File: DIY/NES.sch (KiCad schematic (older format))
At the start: 9 parts, among them J1 Conn_01x07, J2 Conn_01x07, J3 DB15_Female, J4 DB25_Male, U1 74AHCT125N, U2 74AHCT125N

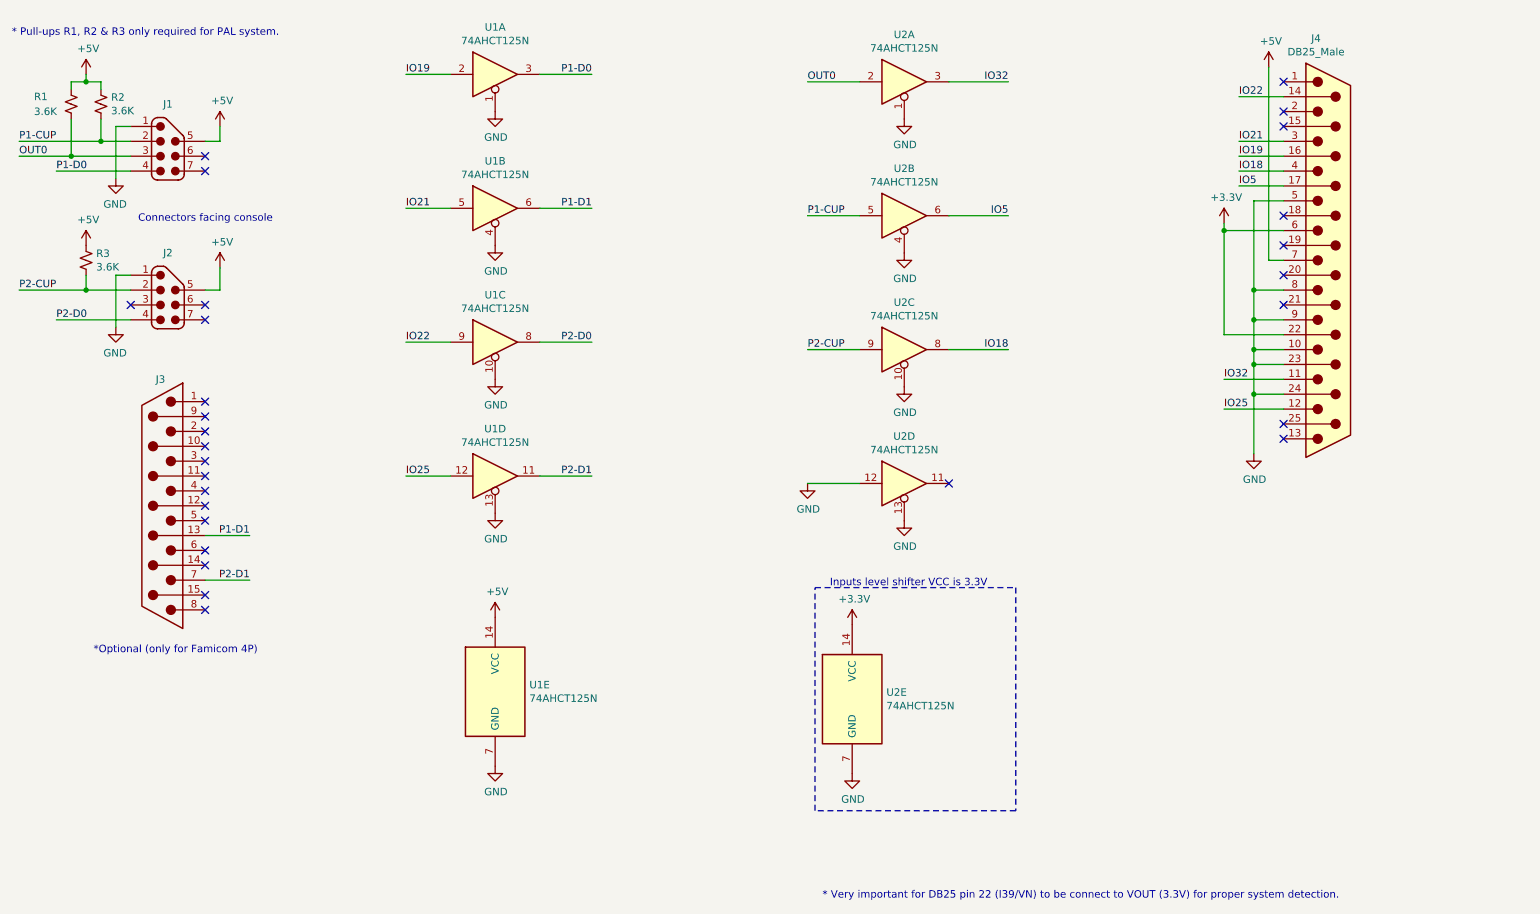
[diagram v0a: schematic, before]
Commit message: Split NES and FC schematic into 3 types
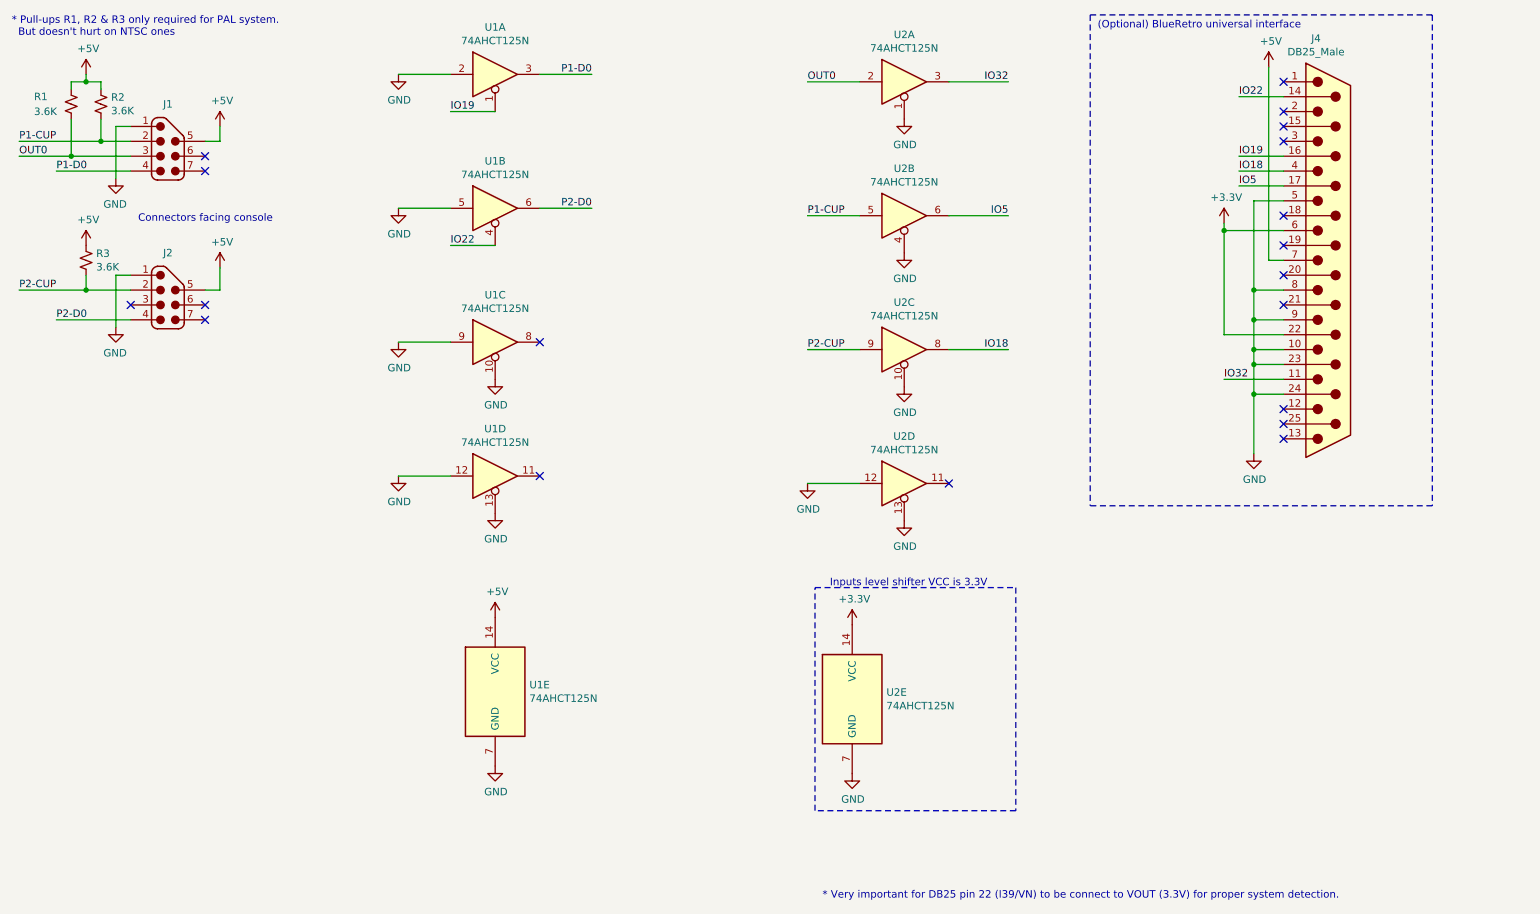
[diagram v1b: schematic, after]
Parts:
- removed J3: DB15_Female, symbol Connector_Gaming:Atari5200_Famicom_NeoGeoAES_PCGamePort_DA15
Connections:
- net P1-D1 is gone; now on net P2-D0: U1.6
- net GND: now also U1.12, U1.2, U1.5, U1.9; no longer U1.1, U1.4
- net IO19: now also U1.1; no longer U1.2
- net IO22: now also U1.4; no longer U1.9
- net P2-D0: no longer U1.8
- net IO21: no longer names the net of J4.3
- net IO21: no longer U1.5
- net IO25: no longer names the net of J4.12
- net IO25: no longer U1.12
- net P2-D1: no longer names the net of U1.11
- no-connect marks 28 -> 19
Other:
- note added: "(Optional) BlueRetro universal interface"
- note added: "* Pull-ups R1, R2 & R3 only required for PAL system.\n But doesn't hurt on NTSC ones"
- note removed: "* Pull-ups R1, R2 & R3 only required for PAL system."
- note removed: "*Optional (only for Famicom 4P)"
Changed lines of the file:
@@
 $Descr USLetter 11000 8500
 encoding utf-8
-Sheet 3 21
-Title "BlueRetro - Famicom/NES adapter cable"
+Sheet 3 23
+Title "BlueRetro - NES adapter cable"
 Date "2020-11-03"
-Rev "v1.2.1"
+Rev "v1.3"
 Comp "©2020-2022 Jacques Gagnon, licensed under CC-BY-4.0"
 Comment1 ""
@@
 $Comp
 L 74xx:74LS125 U?
-U 2 1 5F23BC86
-P 4150 2250
-AR Path="/5F127084/5F23BC86" Ref="U?"  Part="2"
-AR Path="/5F1E85DD/5F23BC86" Ref="U1"  Part="2"
-F 0 "U1" H 4150 2567 50  0000 C CNN
-F 1 "74AHCT125N" H 4150 2476 50  0000 C CNN
-F 2 "" H 4150 2250 50  0001 C CNN
-F 3 "http://www.ti.com/lit/gpn/sn74LS125" H 4150 2250 50  0001 C CNN
-	2    4150 2250
-	1    0    0    -1
-$EndComp
-$Comp
-L 74xx:74LS125 U?
-U 3 1 5F23BC8C
-P 4150 3150
-AR Path="/5F127084/5F23BC8C" Ref="U?"  Part="3"
-AR Path="/5F1E85DD/5F23BC8C" Ref="U1"  Part="3"
-F 0 "U1" H 4150 3467 50  0000 C CNN
-F 1 "74AHCT125N" H 4150 3376 50  0000 C CNN
-F 2 "" H 4150 3150 50  0001 C CNN
-F 3 "http://www.ti.com/lit/gpn/sn74LS125" H 4150 3150 50  0001 C CNN
-	3    4150 3150
-	1    0    0    -1
-$EndComp
-$Comp
-L 74xx:74LS125 U?
 U 4 1 5F23BC92
 P 4150 4050
@@
 F 3 "" H 6900 2550 50  0001 C CNN
 	1    6900 2550
-	1    0    0    -1
-$EndComp
-$Comp
-L power:GND #PWR?
-U 1 1 5F23BD36
-P 4150 2500
-AR Path="/5F127084/5F23BD36" Ref="#PWR?"  Part="1"
-AR Path="/5F1E85DD/5F23BD36" Ref="#PWR049"  Part="1"
-F 0 "#PWR049" H 4150 2250 50  0001 C CNN
-F 1 "GND" H 4155 2327 50  0000 C CNN
-F 2 "" H 4150 2500 50  0001 C CNN
-F 3 "" H 4150 2500 50  0001 C CNN
-	1    4150 2500
-	1    0    0    -1
-$EndComp
-$Comp
-L power:GND #PWR?
-U 1 1 5F23BD3C
-P 4150 4300
-AR Path="/5F127084/5F23BD3C" Ref="#PWR?"  Part="1"
-AR Path="/5F1E85DD/5F23BD3C" Ref="#PWR051"  Part="1"
-F 0 "#PWR051" H 4150 4050 50  0001 C CNN
-F 1 "GND" H 4155 4127 50  0000 C CNN
-F 2 "" H 4150 4300 50  0001 C CNN
-F 3 "" H 4150 4300 50  0001 C CNN
-	1    4150 4300
-	1    0    0    -1
-$EndComp
-$Comp
-L power:GND #PWR?
-U 1 1 5F23BD42
-P 4150 1600
-AR Path="/5F127084/5F23BD42" Ref="#PWR?"  Part="1"
-AR Path="/5F1E85DD/5F23BD42" Ref="#PWR048"  Part="1"
-F 0 "#PWR048" H 4150 1350 50  0001 C CNN
-F 1 "GND" H 4155 1427 50  0000 C CNN
-F 2 "" H 4150 1600 50  0001 C CNN
-F 3 "" H 4150 1600 50  0001 C CNN
-	1    4150 1600
-	1    0    0    -1
-$EndComp
-$Comp
-L power:GND #PWR?
-U 1 1 5F23BD48
-P 4150 3400
-AR Path="/5F127084/5F23BD48" Ref="#PWR?"  Part="1"
-AR Path="/5F1E85DD/5F23BD48" Ref="#PWR050"  Part="1"
-F 0 "#PWR050" H 4150 3150 50  0001 C CNN
-F 1 "GND" H 4155 3227 50  0000 C CNN
-F 2 "" H 4150 3400 50  0001 C CNN
-F 3 "" H 4150 3400 50  0001 C CNN
-	1    4150 3400
 	1    0    0    -1
 $EndComp
@@
 Inputs level shifter VCC is 3.3V
 Wire Wire Line
-	3850 1350 3550 1350
-Wire Wire Line
-	3850 2250 3550 2250
-Wire Wire Line
-	3850 3150 3550 3150
-Wire Wire Line
-	3850 4050 3550 4050
+	4150 1600 3850 1600
 Wire Wire Line
 	4450 1350 4800 1350
-Wire Wire Line
-	4450 2250 4800 2250
-Wire Wire Line
-	4450 3150 4800 3150
-Wire Wire Line
-	4450 4050 4800 4050
 Wire Wire Line
 	6600 1400 6250 1400
@@
 	1    0    0    -1
 $EndComp
-$Comp
-L Connector_Gaming:Atari5200_Famicom_NeoGeoAES_PCGamePort_DA15 J3
-U 1 1 5F2B655C
-P 1900 4250
-F 0 "J3" H 1900 3400 50  0000 C CNN
-F 1 "DB15_Female" H 1806 5151 50  0001 C CNN
-F 2 "" H 1900 4250 50  0001 C CNN
-F 3 " ~" H 1900 4250 50  0001 C CNN
-	1    1900 4250
-	-1   0    0    1
-$EndComp
-Wire Wire Line
-	2200 4450 2500 4450
-Wire Wire Line
-	2200 4750 2500 4750
-Text Notes 1450 5250 0    50   ~ 0
-*Optional (only for Famicom 4P)
-NoConn ~ 2200 3550
-NoConn ~ 2200 3650
-NoConn ~ 2200 3750
-NoConn ~ 2200 3850
-NoConn ~ 2200 3950
-NoConn ~ 2200 4050
-NoConn ~ 2200 4150
-NoConn ~ 2200 4250
-NoConn ~ 2200 4350
-NoConn ~ 2200 4550
-NoConn ~ 2200 4650
-NoConn ~ 2200 4850
-NoConn ~ 2200 4950
-Text Label 2500 4450 2    50   ~ 0
-P1-D1
-Text Label 2500 4750 2    50   ~ 0
-P2-D1
 Wire Wire Line
 	1700 2700 1600 2700
@@
 NoConn ~ 2200 1900
 NoConn ~ 2200 2000
-Text Label 3550 1350 0    50   ~ 0
+Text Label 3850 1600 0    50   ~ 0
 IO19
-Text Label 3550 2250 0    50   ~ 0
-IO21
-Text Label 3550 3150 0    50   ~ 0
-IO22
-Text Label 3550 4050 0    50   ~ 0
-IO25
 Text Label 6250 1400 0    50   ~ 0
 OUT0
@@
 Text Label 4800 1350 2    50   ~ 0
 P1-D0
-Text Label 4800 3150 2    50   ~ 0
-P2-D0
-Text Label 4800 2250 2    50   ~ 0
-P1-D1
-Text Label 4800 4050 2    50   ~ 0
-P2-D1
 Text Label 7600 1400 2    50   ~ 0
 IO32
@@
 $EndComp
 Wire Wire Line
-	9150 1800 9450 1800
-Wire Wire Line
 	9150 2000 9450 2000
 $Comp
@@
 Text Label 9150 1900 0    50   ~ 0
 IO19
-Text Label 9150 1800 0    50   ~ 0
-IO21
 Text Label 9150 1500 0    50   ~ 0
 IO22
-Text Label 9050 3600 0    50   ~ 0
-IO25
 Wire Wire Line
 	9450 2100 9150 2100
@@
 Wire Wire Line
 	9450 1500 9150 1500
-Wire Wire Line
-	9450 3600 9050 3600
 Wire Wire Line
 	9450 3400 9050 3400
@@
 	1300 1900 1700 1900
 Text Notes 900  1100 0    50   ~ 0
-* Pull-ups R1, R2 & R3 only required for PAL system.
+* Pull-ups R1, R2 & R3 only required for PAL system.\n  But doesn't hurt on NTSC ones
+Wire Wire Line
+	3850 1350 3500 1350
+$Comp
+L power:GND #PWR?
+U 1 1 656342E9
+P 3500 1350
+AR Path="/5F127084/656342E9" Ref="#PWR?"  Part="1"
+AR Path="/5F1E85DD/656342E9" Ref="#PWR?"  Part="1"
+F 0 "#PWR?" H 3500 1100 50  0001 C CNN
+F 1 "GND" H 3505 1177 50  0000 C CNN
+F 2 "" H 3500 1350 50  0001 C CNN
+F 3 "" H 3500 1350 50  0001 C CNN
+	1    3500 1350
+	1    0    0    -1
+$EndComp
+Wire Wire Line
+	3850 4050 3500 4050
+$Comp
+L power:GND #PWR?
+U 1 1 656396C9
+P 3500 4050
+AR Path="/5F127084/656396C9" Ref="#PWR?"  Part="1"
+AR Path="/5F1E85DD/656396C9" Ref="#PWR?"  Part="1"
+F 0 "#PWR?" H 3500 3800 50  0001 C CNN
+F 1 "GND" H 3505 3877 50  0000 C CNN
+F 2 "" H 3500 4050 50  0001 C CNN
+F 3 "" H 3500 4050 50  0001 C CNN
+	1    3500 4050
+	1    0    0    -1
+$EndComp
+$Comp
+L power:GND #PWR?
+U 1 1 65637ACC
+P 3500 3150
+AR Path="/5F127084/65637ACC" Ref="#PWR?"  Part="1"
+AR Path="/5F1E85DD/65637ACC" Ref="#PWR?"  Part="1"
+F 0 "#PWR?" H 3500 2900 50  0001 C CNN
+F 1 "GND" H 3505 2977 50  0000 C CNN
+F 2 "" H 3500 3150 50  0001 C CNN
+F 3 "" H 3500 3150 50  0001 C CNN
+	1    3500 3150
+	1    0    0    -1
+$EndComp
+Wire Wire Line
+	3850 3150 3500 3150
+Text Label 4800 2250 2    50   ~ 0
+P2-D0
+Text Label 3850 2500 0    50   ~ 0
+IO22
+$Comp
+L 74xx:74LS125 U?
+U 3 1 5F23BC8C
+P 4150 3150
+AR Path="/5F127084/5F23BC8C" Ref="U?"  Part="3"
+AR Path="/5F1E85DD/5F23BC8C" Ref="U1"  Part="3"
+F 0 "U1" H 4150 3467 50  0000 C CNN
+F 1 "74AHCT125N" H 4150 3376 50  0000 C CNN
+F 2 "" H 4150 3150 50  0001 C CNN
+F 3 "http://www.ti.com/lit/gpn/sn74LS125" H 4150 3150 50  0001 C CNN
+	3    4150 3150
+	1    0    0    -1
+$EndComp
+$Comp
+L power:GND #PWR?
+U 1 1 65635E7D
+P 3500 2250
+AR Path="/5F127084/65635E7D" Ref="#PWR?"  Part="1"
+AR Path="/5F1E85DD/65635E7D" Ref="#PWR?"  Part="1"
+F 0 "#PWR?" H 3500 2000 50  0001 C CNN
+F 1 "GND" H 3505 2077 50  0000 C CNN
+F 2 "" H 3500 2250 50  0001 C CNN
+F 3 "" H 3500 2250 50  0001 C CNN
+	1    3500 2250
+	1    0    0    -1
+$EndComp
+Wire Wire Line
+	3850 2250 3500 2250
+Wire Wire Line
+	4450 2250 4800 2250
+Wire Wire Line
+	4150 2500 3850 2500
+$Comp
+L 74xx:74LS125 U?
+U 2 1 5F23BC86
+P 4150 2250
+AR Path="/5F127084/5F23BC86" Ref="U?"  Part="2"
+AR Path="/5F1E85DD/5F23BC86" Ref="U1"  Part="2"
+F 0 "U1" H 4150 2567 50  0000 C CNN
+F 1 "74AHCT125N" H 4150 2476 50  0000 C CNN
+F 2 "" H 4150 2250 50  0001 C CNN
+F 3 "http://www.ti.com/lit/gpn/sn74LS125" H 4150 2250 50  0001 C CNN
+	2    4150 2250
+	1    0    0    -1
+$EndComp
+$Comp
+L power:GND #PWR?
+U 1 1 6567C781
+P 4150 4300
+AR Path="/5F127084/6567C781" Ref="#PWR?"  Part="1"
+AR Path="/5F1E85DD/6567C781" Ref="#PWR?"  Part="1"
+F 0 "#PWR?" H 4150 4050 50  0001 C CNN
+F 1 "GND" H 4155 4127 50  0000 C CNN
+F 2 "" H 4150 4300 50  0001 C CNN
+F 3 "" H 4150 4300 50  0001 C CNN
+	1    4150 4300
+	1    0    0    -1
+$EndComp
+$Comp
+L power:GND #PWR?
+U 1 1 6567CAF2
+P 4150 3400
+AR Path="/5F127084/6567CAF2" Ref="#PWR?"  Part="1"
+AR Path="/5F1E85DD/6567CAF2" Ref="#PWR?"  Part="1"
+F 0 "#PWR?" H 4150 3150 50  0001 C CNN
+F 1 "GND" H 4155 3227 50  0000 C CNN
+F 2 "" H 4150 3400 50  0001 C CNN
+F 3 "" H 4150 3400 50  0001 C CNN
+	1    4150 3400
+	1    0    0    -1
+$EndComp
+NoConn ~ 4450 3150
+NoConn ~ 4450 4050
+Wire Notes Line
+	8150 950  10450 950
+Wire Notes Line
+	10450 4250 8150 4250
+Text Notes 8200 1050 0    50   ~ 0
+(Optional) BlueRetro universal interface
+Wire Notes Line
+	10450 950  10450 4250
+Wire Notes Line
+	8150 950  8150 4250
+NoConn ~ 9450 1800
+NoConn ~ 9450 3600
 $EndSCHEMATC

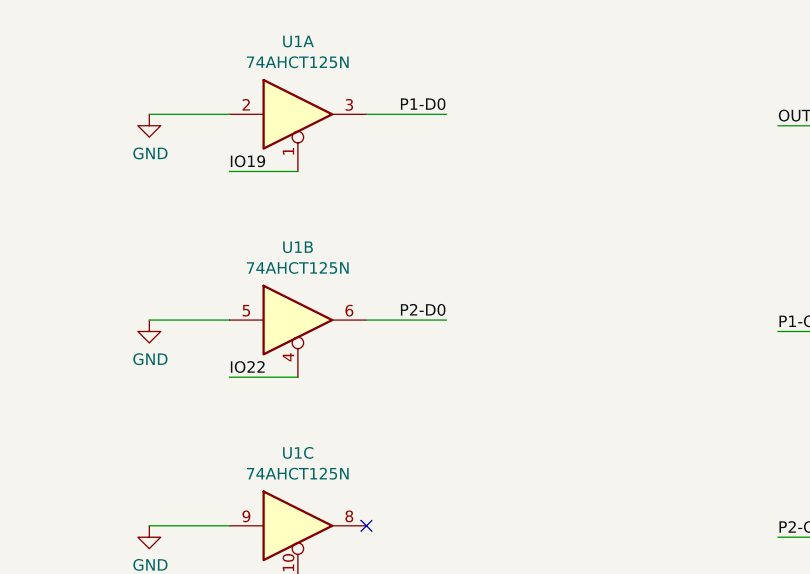
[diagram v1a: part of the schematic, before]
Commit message: Add pullup to OD outputs on ESP side
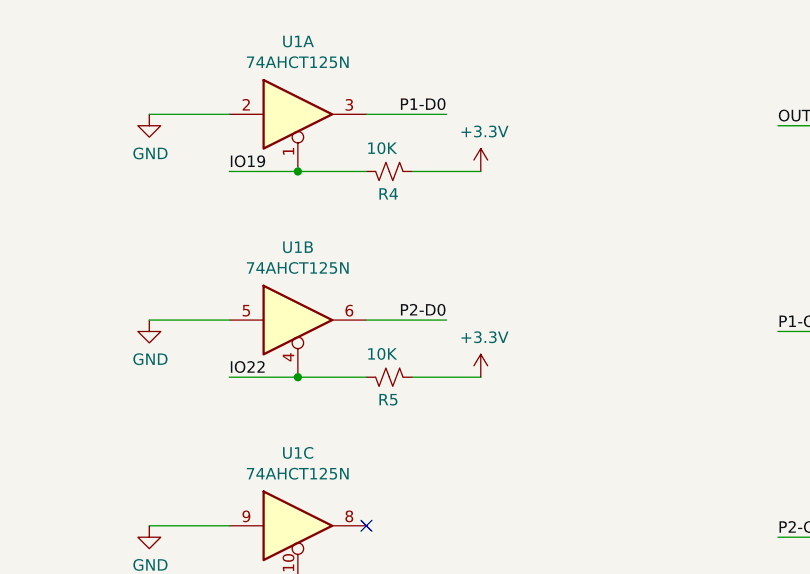
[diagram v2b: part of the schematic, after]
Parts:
- added R4, R5: 10K, symbol Device:R_Small_US
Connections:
- net +3V3: now also R4.1, R5.1
- net IO19: now also R4.2
- net IO22: now also R5.2
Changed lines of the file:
@@
 NoConn ~ 9450 1800
 NoConn ~ 9450 3600
+$Comp
+L power:+3.3V #PWR?
+U 1 1 661DD094
+P 4950 1600
+AR Path="/5F127084/661DD094" Ref="#PWR?"  Part="1"
+AR Path="/5F1E85DD/661DD094" Ref="#PWR?"  Part="1"
+F 0 "#PWR?" H 4950 1450 50  0001 C CNN
+F 1 "+3.3V" H 4965 1773 50  0000 C CNN
+F 2 "" H 4950 1600 50  0001 C CNN
+F 3 "" H 4950 1600 50  0001 C CNN
+	1    4950 1600
+	1    0    0    -1
+$EndComp
+$Comp
+L Device:R_Small_US R4
+U 1 1 661DDE29
+P 4550 1600
+F 0 "R4" V 4450 1550 50  0000 L CNN
+F 1 "10K" V 4650 1500 50  0000 L CNN
+F 2 "" H 4550 1600 50  0001 C CNN
+F 3 "~" H 4550 1600 50  0001 C CNN
+	1    4550 1600
+	0    1    -1   0
+$EndComp
+Wire Wire Line
+	4150 1600 4450 1600
+Connection ~ 4150 1600
+Wire Wire Line
+	4650 1600 4950 1600
+$Comp
+L power:+3.3V #PWR?
+U 1 1 661E3A89
+P 4950 2500
+AR Path="/5F127084/661E3A89" Ref="#PWR?"  Part="1"
+AR Path="/5F1E85DD/661E3A89" Ref="#PWR?"  Part="1"
+F 0 "#PWR?" H 4950 2350 50  0001 C CNN
+F 1 "+3.3V" H 4965 2673 50  0000 C CNN
+F 2 "" H 4950 2500 50  0001 C CNN
+F 3 "" H 4950 2500 50  0001 C CNN
+	1    4950 2500
+	1    0    0    -1
+$EndComp
+$Comp
+L Device:R_Small_US R5
+U 1 1 661E3A8F
+P 4550 2500
+F 0 "R5" V 4450 2450 50  0000 L CNN
+F 1 "10K" V 4650 2400 50  0000 L CNN
+F 2 "" H 4550 2500 50  0001 C CNN
+F 3 "~" H 4550 2500 50  0001 C CNN
+	1    4550 2500
+	0    1    -1   0
+$EndComp
+Wire Wire Line
+	4650 2500 4950 2500
+Wire Wire Line
+	4450 2500 4150 2500
+Connection ~ 4150 2500
 $EndSCHEMATC
